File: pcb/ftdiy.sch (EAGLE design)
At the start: 2 parts, among them U1 CP2108

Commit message: Finish schematic, board and generate gerbers
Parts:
- added C1, C5: 1uF, Capacitor:CAPACITOR-0603
- added C2, C3, C4: 100nF, Capacitor:CAPACITOR-0603
- added D1: SP0503BAHT, TVS:SP0503BAHT
- added D10: RED, LED:LED0603
- added D2, D4, D7, D9: GREEN, LED:LED0603
- added D3, D5, D6, D8: BLUE, LED:LED0603
- added F1: 500mA, PTC Fuses:PTC1206
- added JP1, JP2, JP3, JP4: PINHD-1X6, Pin Header:PINHD-1X6
- added JP5: PINHD-2X3, Pin Header:PINHD-2X3
- added R1: 10K Ohms, Resistor:RESISTOR-0603
- added R10, R2, R3, R4, R5, R6, R7, R8, R9: 330 Ohms, Resistor:RESISTOR-0603
- USB1: value USB_ID_6_SHIELD-MICRO-B-SMT -> USB-MICRO-B-SMD-FLAT-SIDE; device USB Connector:USB_ID_6_SHIELD-MICRO-B-SMT -> USB Connector:USB-MICRO-B-SMD-FLAT-SIDE
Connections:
- new net !P0_RX_LED: D3.C, U1.CTL.GPIO1
- new net !P0_TX_LED: D2.C, U1.CTL.GPIO0
- new net !P1_RX_LED: D5.C, U1.CTL.GPIO5
- new net !P1_TX_LED: D4.C, U1.CTL.GPIO4
- new net !P2_RX_LED: D7.C, U1.CTL.GPIO9
- new net !P2_TX_LED: D6.C, U1.CTL.GPIO8
- new net !P3_RX_LED: D9.C, U1.CTL.GPIO13
- new net !P3_TX_LED: D8.C, U1.CTL.GPIO12
- new net 3V3: C3.C1, C4.C1, C5.C1, JP5-3.S, JP5-4.S, R1.2, U1.CTL.VDD, U1.CTL.VIO@0, U1.CTL.VIO@1
- new net 5V0: C1.C1, C2.C1, D1.4, F1.1, JP5-1.S, JP5-2.S, R10.2, R2.2, R3.2, R4.2, R5.2, R6.2, R7.2, R8.2, R9.2, U1.CTL.VBUS, U1.CTL.VIOHD, U1.CTL.VREGIN
- new net D+: D1.2, U1.CTL.D+, USB1.D+
- new net D-: D1.3, U1.CTL.D-, USB1.D-
- new net GND: C1.C2, C2.C2, C3.C2, C4.C2, C5.C2, D1.1, JP1-1.S, JP2-1.S, JP3-1.S, JP4-1.S, JP5-5.S, JP5-6.S, U1.CTL.VSS@0, U1.CTL.VSS@1, U1.CTL.VSS@2, U1.CTL.VSSHD, USB1.GND, USB1.SHIELD@0, USB1.SHIELD@1, USB1.SHIELD@2, USB1.SHIELD@3, USB1.SHIELD@4, USB1.SHIELD@5
- new net N$1: JP1-2.S, U1.P0.RX
- new net N$10: JP2-6.S, U1.P1.DTR
- new net N$11: JP3-2.S, U1.P2.RX
- new net N$12: JP3-3.S, U1.P2.TX
- new net N$13: JP3-4.S, U1.P2.RTS
- new net N$14: JP3-5.S, U1.P2.CTS
- new net N$15: JP3-6.S, U1.P2.DTR
- new net N$16: JP4-2.S, U1.P3(HD).RX
- new net N$17: JP4-3.S, U1.P3(HD).TX
- new net N$18: JP4-4.S, U1.P3(HD).RTS
- new net N$19: JP4-5.S, U1.P3(HD).CTS
- new net N$2: JP1-3.S, U1.P0.TX
- new net N$20: JP4-6.S, U1.P3(HD).DTR
- new net N$21: R1.1, U1.CTL.!RST
- new net N$22: D10.A, R2.1
- new net N$23: D2.A, R3.1
- new net N$24: D3.A, R4.1
- new net N$25: D4.A, R5.1
- new net N$26: D5.A, R6.1
- new net N$27: D6.A, R7.1
- new net N$28: D7.A, R8.1
- new net N$29: D8.A, R9.1
- new net N$3: JP1-4.S, U1.P0.RTS
- new net N$30: D9.A, R10.1
- new net N$31: F1.2, USB1.VBUS
- new net N$4: JP1-5.S, U1.P0.CTS
- new net N$5: JP1-6.S, U1.P0.DTR
- new net N$6: JP2-2.S, U1.P1.RX
- new net N$7: JP2-3.S, U1.P1.TX
- new net N$8: JP2-4.S, U1.P1.RTS
- new net N$9: JP2-5.S, U1.P1.CTS
- new net PWR_LED: D10.C, U1.CTL.SUSPEND
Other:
- moved on the sheet: U1.CTL, U1.P0, U1.P1, U1.P2, U1.P3(HD), USB1

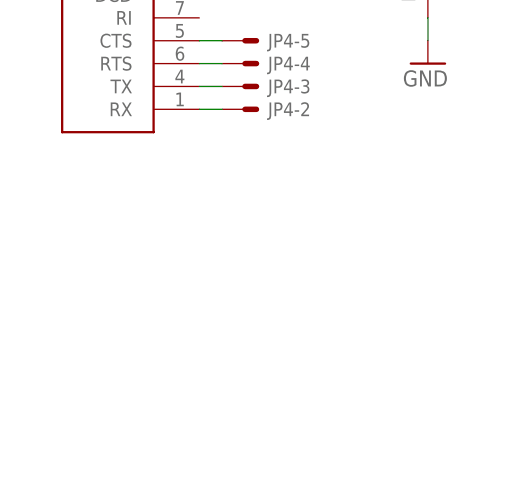
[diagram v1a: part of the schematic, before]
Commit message: Add OSHW logo
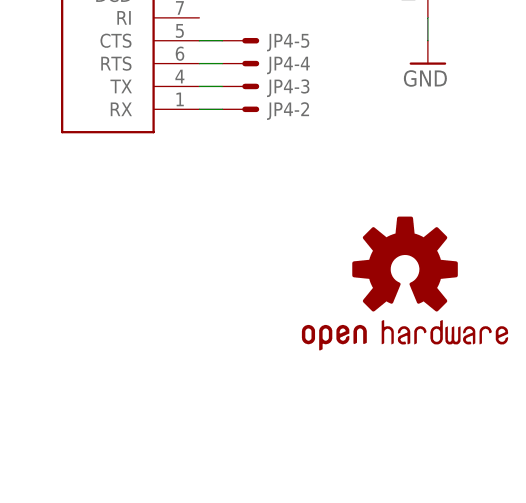
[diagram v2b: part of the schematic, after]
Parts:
- added LOGO1: OSHW-LOGOM, Silkscreen:OSHW-LOGOM
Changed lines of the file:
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@@
 <part name="5V5" library="Supply Symbol" deviceset="5V0" device=""/>
 <part name="3V6" library="Supply Symbol" deviceset="3V3" device=""/>
+<part name="LOGO1" library="Silkscreen" deviceset="OSHW-LOGO" device="M"/>
 </parts>
 <sheets>
@@
 <attribute name="VALUE" x="134.62" y="33.02" size="1.778" layer="96" rot="R90"/>
 </instance>
+<instance part="LOGO1" gate="G$1" x="241.3" y="35.56" smashed="yes"/>
 </instances>
 <busses>
